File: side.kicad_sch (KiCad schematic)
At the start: 80 parts, among them J1 Conn_01x02, J2 SWD_Connector, J3 USB_C_Receptacle_USB2.0_16P, SW1 Reset Button, SW10 SW_Push, SW11 SW_Push, SW12 SW_Push, SW13 SW_Push, SW14 SW_Push, SW15 SW_Push, SW16 SW_Push, SW17 SW_Push, SW18 SW_Push, SW19 SW_Push, SW20 SW_Push, SW21 SW_Push, SW22 SW_Push, SW23 SW_Push, SW3 SW_Push, SW4 SW_Push, SW5 SW_Push, SW6 SW_Push, SW7 SW_Push, SW8 SW_Push, SW9 SW_Push, U2 USBLC6-2SC6, U7 nRF52833_QDxx, Y1 32MHz, Y3 32.768 kHz

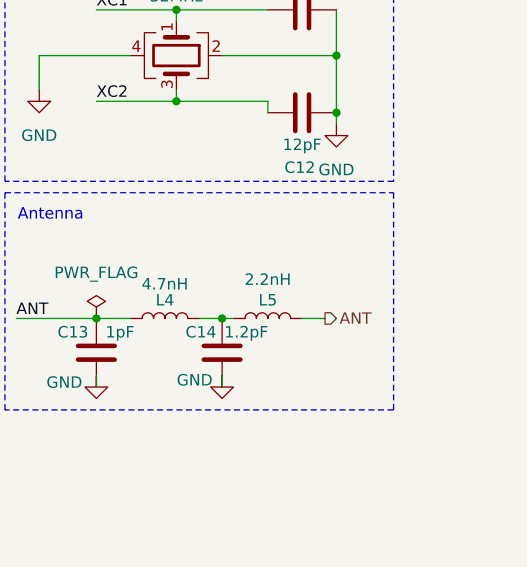
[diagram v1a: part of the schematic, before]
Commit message: switched to chip antenna
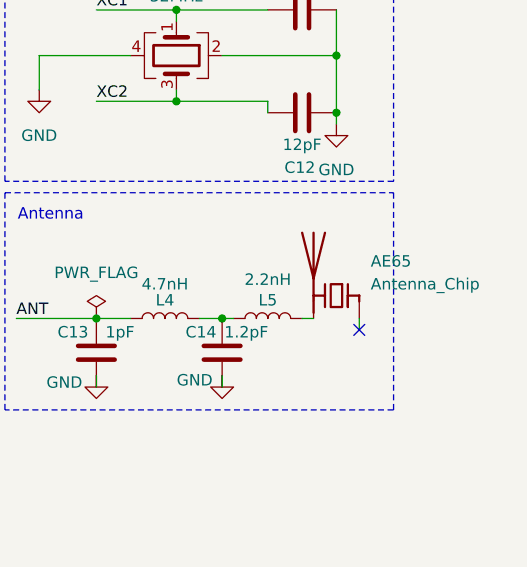
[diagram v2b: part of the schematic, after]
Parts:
- added AE65: Antenna_Chip, 2450AT42A100E:ANTC5020X110N, symbol Device:Antenna_Chip
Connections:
- net ANT: no longer L5.2
- new net: AE65.2 (PCB_Trace), L5.2
- no-connect marks 6 -> 7
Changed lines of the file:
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@@
 	)
 	(no_connect
+		(at 278.13 156.21)
+	)
+	(no_connect
 		(at 134.62 186.69)
 	)
@@
 	(wire
 		(pts
-			(xy 271.78 154.94) (xy 274.32 154.94)
+			(xy 271.78 154.94) (xy 273.05 154.94)
 		)
 		(stroke
@@
 	(wire
 		(pts
+			(xy 278.13 156.21) (xy 278.13 154.94)
+		)
+		(stroke
+			(width 0)
+			(type default)
+		)
+	)
+	(wire
+		(pts
 			(xy 214.63 81.28) (xy 214.63 95.25)
 		)
@@
 		)
 	)
-	(hierarchical_label "ANT"
-		(shape output)
-		(at 274.32 154.94 0)
-		(fields_autoplaced yes)
-		(effects
-			(font
-				(size 1.27 1.27)
-			)
-			(justify left)
-		)
-	)
 	(symbol
 		(lib_id "Switch:SW_Push")
@@
 					(unit 1)
 				)
+			)
+		)
+	)
+	(symbol
+		(lib_id "Device:Antenna_Chip")
+		(at 275.59 152.4 0)
+		(mirror y)
+		(unit 1)
+		(exclude_from_sim no)
+		(in_bom yes)
+		(on_board yes)
+		(dnp no)
+		(fields_autoplaced yes)
+		(property "Reference" "AE65"
+			(at 279.4 148.5899 0)
+			(effects
+				(font
+					(size 1.27 1.27)
+				)
+				(justify right)
+			)
+		)
+		(property "Value" "Antenna_Chip"
+			(at 279.4 151.1299 0)
+			(effects
+				(font
+					(size 1.27 1.27)
+				)
+				(justify right)
+			)
+		)
+		(property "Footprint" "2450AT42A100E:ANTC5020X110N"
+			(at 278.13 147.955 0)
+			(effects
+				(font
+					(size 1.27 1.27)
+				)
+				(hide yes)
+			)
+		)
+		(property "Datasheet" "~"
+			(at 278.13 147.955 0)
+			(effects
+				(font
+					(size 1.27 1.27)
+				)
+				(hide yes)
+			)
+		)
+		(property "Description" "Ceramic chip antenna with pin for PCB trace"
+			(at 275.59 152.4 0)
+			(effects
+				(font
+					(size 1.27 1.27)
+				)
+				(hide yes)
+			)
+		)
+		(property "LCSC" "C2917719"
+			(at 275.59 152.4 0)
+			(effects
+				(font
+					(size 1.27 1.27)
+				)
+				(hide yes)
+			)
+		)
+		(pin "1"
+		)
+		(pin "2"
+		)
+		(instances
+			(project ""
+				(path "/2b736a6b-c6e2-42fa-94c9-e384d663659b/4bb325fd-7371-4bed-a032-a434391e94c9"
+					(reference "AE65")
+					(unit 1)
+				)
+				(path "/2b736a6b-c6e2-42fa-94c9-e384d663659b/8d53595d-91b9-4d70-adec-5245477c92d0"
+					(reference "AE66")
+					(unit 1)
+				)

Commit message: added lcsc part numbers
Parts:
- C10, C19: LCSC (none) -> C1705
- C11, C12, C15, C31: LCSC (none) -> C106201
- C13: footprint Capacitor_SMD:C_0603_1608Metric -> Capacitor_SMD:C_0402_1005Metric; LCSC (none) -> C309455
- C14: footprint Capacitor_SMD:C_0603_1608Metric -> Capacitor_SMD:C_0402_1005Metric; LCSC (none) -> C327292
- C2: footprint Capacitor_SMD:C_0603_1608Metric -> Capacitor_SMD:C_0402_1005Metric; LCSC (none) -> C60474
- C39, C7: LCSC (none) -> C14445
- C4, C41, C43: LCSC (none) -> C60474
- C5: LCSC (none) -> C77177
- C6: LCSC (none) -> C107031
- C9: LCSC (none) -> C307423
- D10, D11, D12, D13, D14, D15, D16, D17, D18, D19, D2, D20, D21, D22, D3, D4, D5, D6, D7, D8, D9: LCSC (none) -> C963381
- J1, J2: now left out of the parts list
- L4: LCSC (none) -> C86065
- L5: LCSC (none) -> C86061
- R1: LCSC (none) -> C60491
- R2: LCSC (none) -> C3016043
- R3: LCSC (none) -> C11512
- R4, R5: LCSC (none) -> C25905
- SW1: LCSC (none) -> C2886897
- SW10, SW11, SW12, SW13, SW14, SW15, SW16, SW17, SW18, SW19, SW20, SW21, SW22, SW23, SW3, SW4, SW5, SW6, SW7, SW8, SW9: LCSC (none) -> C5333465
- U2: LCSC (none) -> C7519
- U7: LCSC C2895249 -> C2895249
- Y1: LCSC C2149238 -> C2149238
